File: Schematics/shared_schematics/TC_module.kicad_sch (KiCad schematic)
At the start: 13 parts, among them J7 Screw_Terminal_01x02

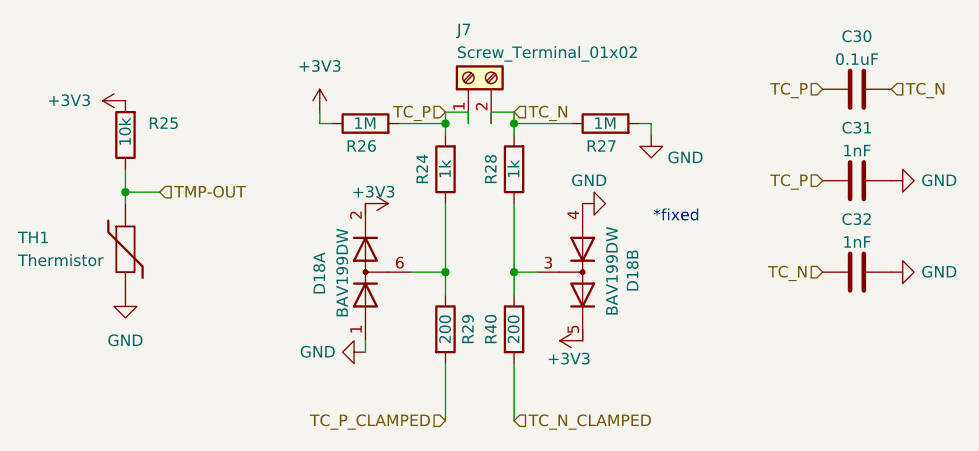
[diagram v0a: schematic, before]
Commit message: add decoupling, revise power circuitry (ferrite bead, LDO swap), merge shared-schemtic branch changes.
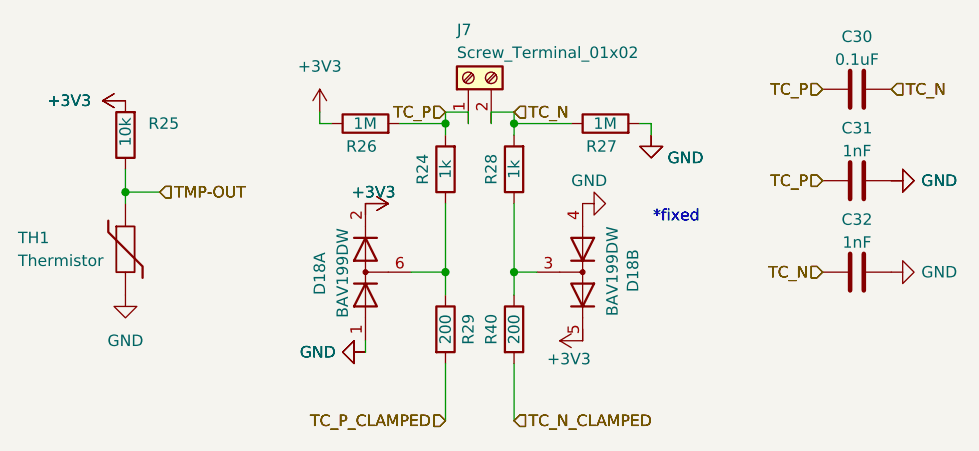
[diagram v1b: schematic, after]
